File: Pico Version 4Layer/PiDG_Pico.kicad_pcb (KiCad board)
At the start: 4 copper layers, 126 x 126 mm, 49 parts, among them J1 Conn_02x05_Odd_Even, J10 Trig, J11 Laser Enable, J12 Pixel Reset, J14 Pico Socket A, J15 Pico Socket B, J16 Laser En/PWM Trig/GND, J2 Conn_02x05_Odd_Even, J3 Conn_02x05_Odd_Even, J4 Conn_02x05_Odd_Even, J5 Conn_02x05_Odd_Even, J6 Conn_02x05_Odd_Even, J7 Laser 1, J8 Laser 2, U1 74LVC1G04, U10 74AHCT1G08, U12 74LVC1G17, U13 UCC27524, U2 SN74LVC04AD, U3 74LVC1G04, U4 SN74LVC04AD, U5 74LVC1G04, U6 SN74LVC04AD, U7 74AHCT1G08, U8 74AHCT1G08, U9 NCP718xSN180

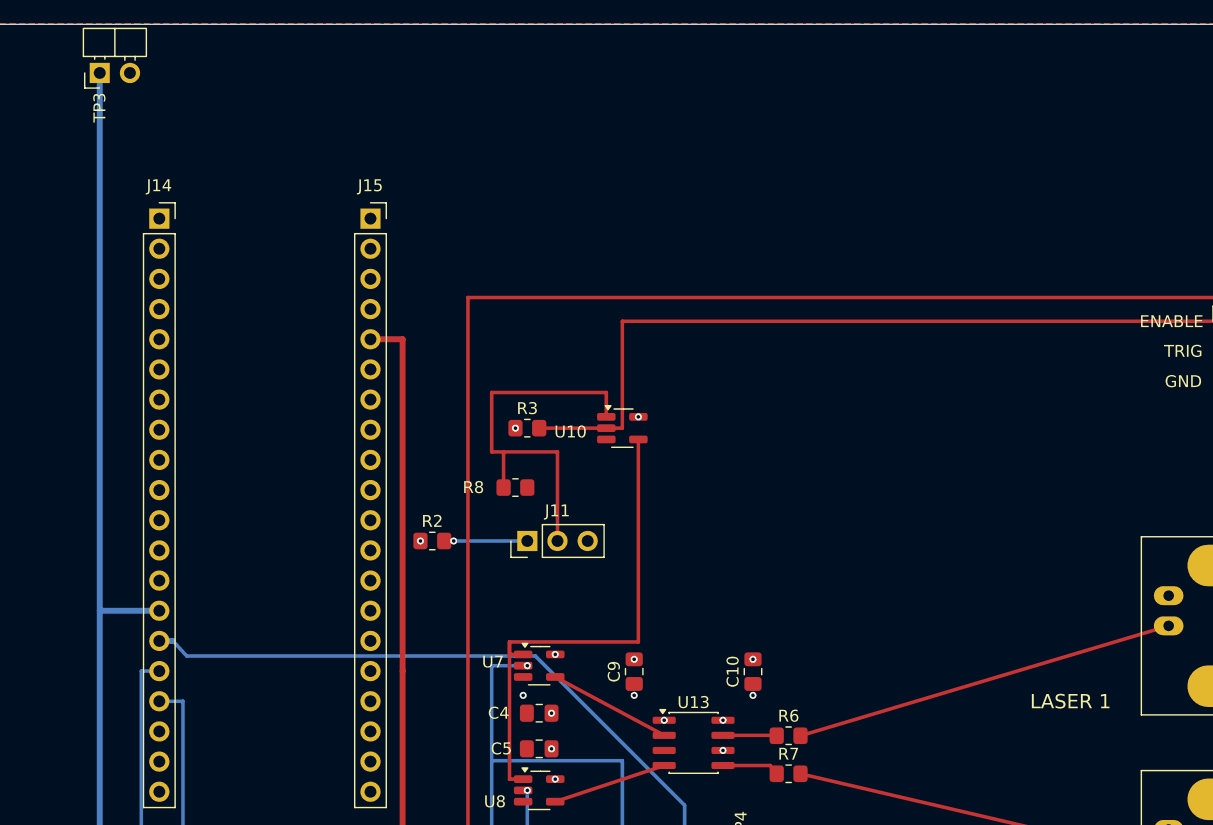
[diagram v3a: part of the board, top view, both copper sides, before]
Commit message: USB-C PD power input: 12 V laser-driver rail and 5 V into the VSYS plane
J17 (USB-C, power only) + U14 CH224K request 15 V from a PD charger.
- U15 AP63205WU buck + U16 LM66100 ideal diode feed the +5V plane (Pico
  VSYS). CE tied to VOUT for reverse blocking.
- U17 LP2951 (adjustable, R12/R13 100k/11.3k 0.1 %) makes 12.0 V for the
  UCC27524. R14 1R gives the output ESR both TI LP2951 dies need.
- U17 ~ERROR drives U13 ENA/ENB (LASER_PWR_OK, R16 pull-up): outputs are
  held low with no PD, before the contract, and on 5 V/9 V chargers.
- R6/R7 47 -> 69.8 ohm: worst-case 4.55-5.16 V into the 50 ohm LDP-V
  trigger input (was ~2.4 V). C10 -> 10 uF 1206 on +12V.
- Pico VBUS (J15.1) disconnected from +5V; USB now reaches VSYS only
  through the Pico's own Schottky, so J17 cannot back-feed the host.
- R17/R18 10k pull-downs on the laser pulse nets: J17 can now power the
  board with the Pico removed.

ERC 0, DRC 0, 0 unconnected; 323 pads match the schematic netlist.
BOM/CPL regenerated (the CPL also picks up the AHCT values it had missed),
fab outputs regenerated, Hardware.md updated.

Co-Authored-By: Claude Opus 5.5 (1M context) <noreply@anthropic.com>
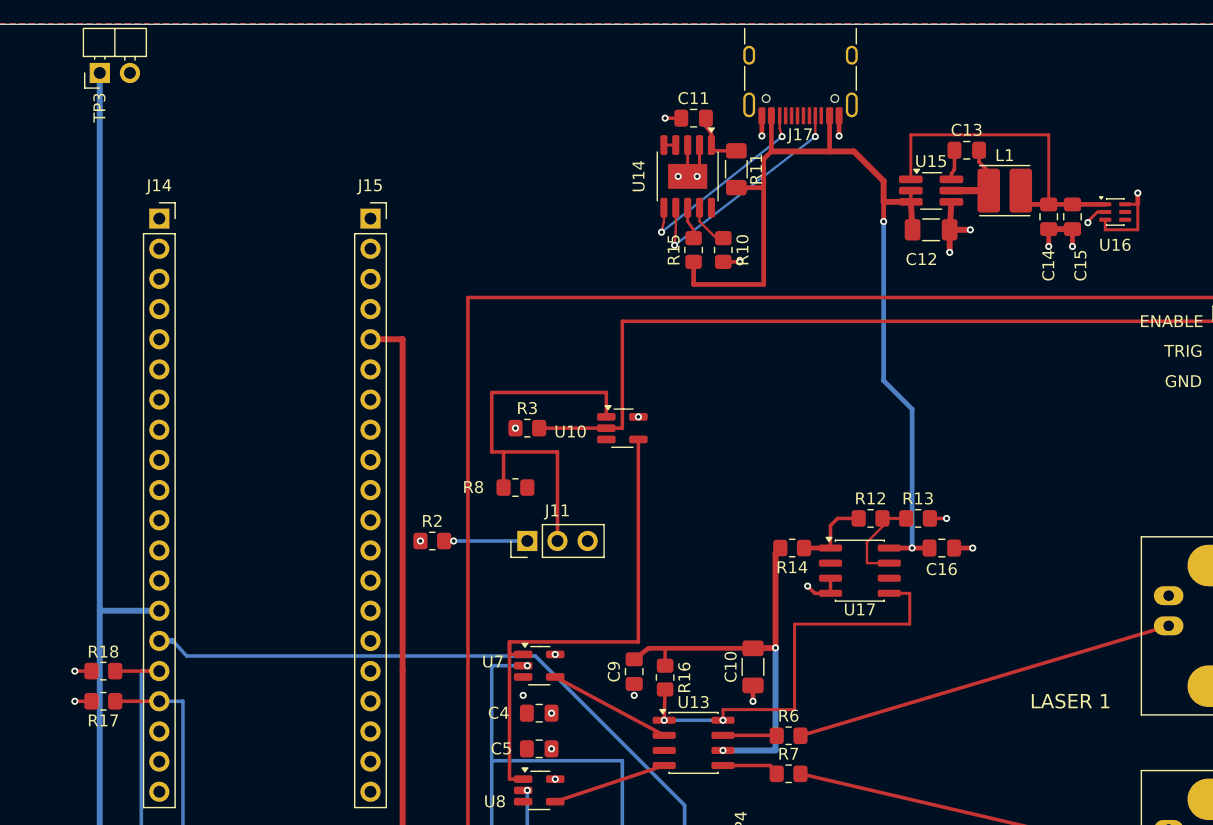
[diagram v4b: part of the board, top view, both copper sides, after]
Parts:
- added C11: 1uF, Capacitor_SMD:C_0805_2012Metric_Pad1.18x1.45mm_HandSolder, F.Cu at (205.0, 37.9)
- added C12: 10uF 50V, Capacitor_SMD:C_1206_3216Metric_Pad1.33x1.80mm_HandSolder, F.Cu at (225.0, 47.3)
- added C13: 0.1uF, Capacitor_SMD:C_0805_2012Metric_Pad1.18x1.45mm_HandSolder, F.Cu at (228.0, 40.6)
- added C14: 22uF, Capacitor_SMD:C_0805_2012Metric_Pad1.18x1.45mm_HandSolder, F.Cu at (234.9, 46.2)
- added C15: 22uF, Capacitor_SMD:C_0805_2012Metric_Pad1.18x1.45mm_HandSolder, F.Cu at (236.9, 46.2)
- added C16: 1uF, Capacitor_SMD:C_0805_2012Metric_Pad1.18x1.45mm_HandSolder, F.Cu at (225.9, 74.1)
- added J17: USB-C PD in, PiDG_Local:USB_C_Receptacle_HRO_TYPE-C-31-M-12_EdgeTrim, F.Cu at (214.0, 33.6)
- added L1: 4.7uH, Inductor_SMD:L_Cenker_CKCS4030, F.Cu at (231.2, 44.0)
- added R10: 56k, Resistor_SMD:R_0805_2012Metric_Pad1.20x1.40mm_HandSolder, F.Cu at (207.5, 49.0)
- added R11: 1k, Resistor_SMD:R_1206_3216Metric_Pad1.30x1.75mm_HandSolder, F.Cu at (208.6, 42.2)
- added R12: 100k, Resistor_SMD:R_0805_2012Metric_Pad1.20x1.40mm_HandSolder, F.Cu at (219.9, 71.6)
- added R13: 11.3k, Resistor_SMD:R_0805_2012Metric_Pad1.20x1.40mm_HandSolder, F.Cu at (223.9, 71.6)
- added R14: 1R, Resistor_SMD:R_0805_2012Metric_Pad1.20x1.40mm_HandSolder, F.Cu at (213.3, 74.1)
- added R15: 10k, Resistor_SMD:R_0805_2012Metric_Pad1.20x1.40mm_HandSolder, F.Cu at (205.0, 49.0)
- added R16: 100k, Resistor_SMD:R_0805_2012Metric_Pad1.20x1.40mm_HandSolder, F.Cu at (202.6, 85.0)
- added R17: 10k, Resistor_SMD:R_0805_2012Metric_Pad1.20x1.40mm_HandSolder, F.Cu at (155.3, 87.0)
- added R18: 10k, Resistor_SMD:R_0805_2012Metric_Pad1.20x1.40mm_HandSolder, F.Cu at (155.3, 84.5)
- added U14: CH224K, Package_SO:SSOP-10-1EP_3.9x4.9mm_P1mm_EP2.1x3.3mm, F.Cu at (204.5, 42.8)
- added U15: AP63205WU, Package_TO_SOT_SMD:TSOT-23-6_HandSoldering, F.Cu at (225.0, 44.0)
- added U16: LM66100, Package_TO_SOT_SMD:SOT-363_SC-70-6, F.Cu at (240.5, 45.8)
- added U17: LP2951D, Package_SO:SOIC-8_3.9x4.9mm_P1.27mm, F.Cu at (219.0, 76.0)
- C10: value 1uF -> 10uF 25V; footprint Capacitor_SMD:C_0805_2012Metric_Pad1.18x1.45mm_HandSolder -> Capacitor_SMD:C_1206_3216Metric_Pad1.33x1.80mm_HandSolder
- R6, R7: value 47 -> 69.8
- moved C10 0.40 mm to (210.0, 84.1)
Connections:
- C10 pad 2: +5V -> +12V
- C9 pad 2: +5V -> +12V
- J15 pad 1: +5V -> unconnected-(J15-Pin_1-Pad1)
- U13 pad 1: +5V -> LASER_PWR_OK
- U13 pad 6: +5V -> +12V
- U13 pad 8: +5V -> LASER_PWR_OK
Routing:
- net VBUS_PD: track 0.00 -> 78.9 mm, vias 0 -> 2
- net LASER_PWR_OK: track 0.00 -> 35.7 mm, vias 0 -> 2
- net +12V: track 0.00 -> 35.3 mm, vias 0 -> 2
- net GND: track 4.28 -> 39.1 mm, vias 13 -> 29
- net +5V_PD: track 0.00 -> 29.5 mm
- net Net-(J17-CC1): track 0.00 -> 19.9 mm, vias 0 -> 2
- net Net-(J17-CC2): track 0.00 -> 16.8 mm, vias 0 -> 2
- net FB12: track 0.00 -> 8.18 mm
- net +5V: track 11.2 -> 18.9 mm, vias 13 -> 9
- net Net-(U15-SW): track 0.00 -> 6.88 mm
- net LDO12_OUT: track 0.00 -> 6.74 mm
- net Net-(U14-VDD): track 0.00 -> 4.31 mm
- net Net-(U14-CFG1): track 0.00 -> 3.74 mm
- net _PULSE_OUT_CH2: track 79.2 -> 82.9 mm
- net _PULSE_OUT_CH1: track 78.3 -> 82.1 mm
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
